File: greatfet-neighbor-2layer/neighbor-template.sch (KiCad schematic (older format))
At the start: 13 parts, among them J1 NEIGHBOR1, J2 NEIGHBOR2, J7 BONUS_ROW, U1 M24C02-FMN6TP

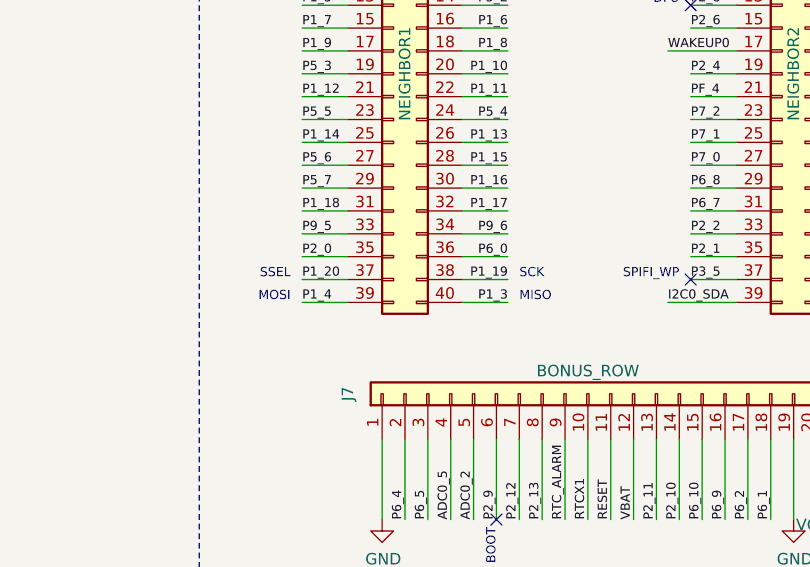
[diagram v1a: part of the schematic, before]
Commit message: adopt OSHWA convention for SPI signal names https://www.oshwa.org/a-resolution-to-redefine-spi-signal-names
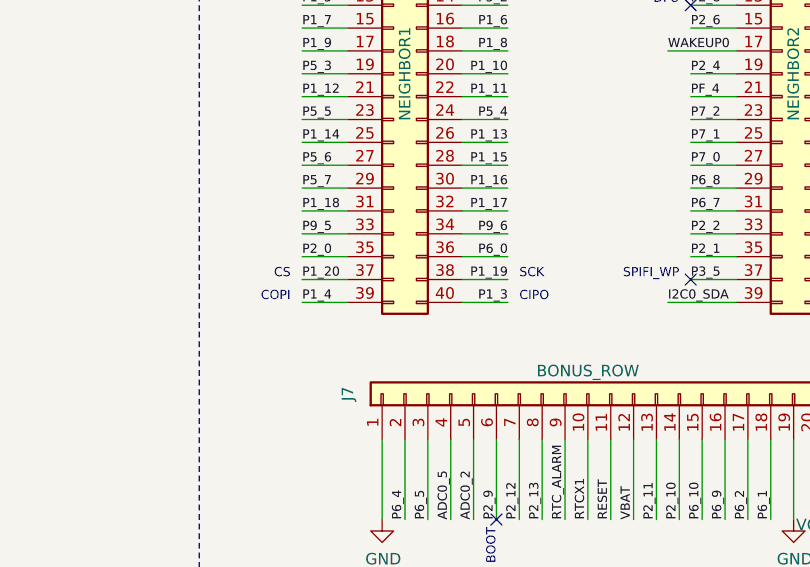
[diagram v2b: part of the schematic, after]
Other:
- note added: "CIPO"
- note added: "COPI"
- note added: "CS"
- note removed: "MISO"
- note removed: "MOSI"
- note removed: "SSEL"
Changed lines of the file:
@@
 P2_0
 Text Notes 14300 2850 0    40   ~ 0
-MISO
+CIPO
 Text Notes 13300 2850 2    40   ~ 0
-MOSI
+COPI
 Text Notes 14300 2750 0    40   ~ 0
 SCK
 Text Notes 13300 2750 2    40   ~ 0
-SSEL
+CS
 Text Label 16050 2850 2    40   ~ 0
 I2C0_SCL

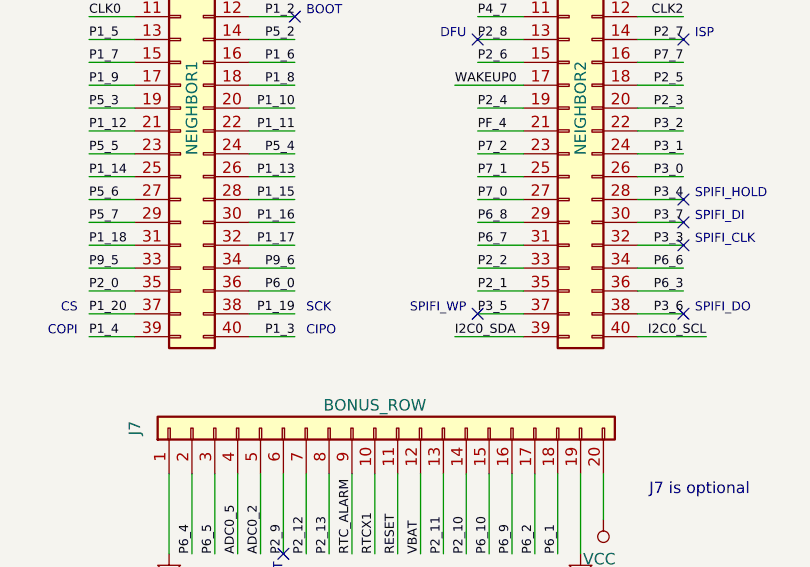
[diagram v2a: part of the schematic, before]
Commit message: label EEPROM_WC
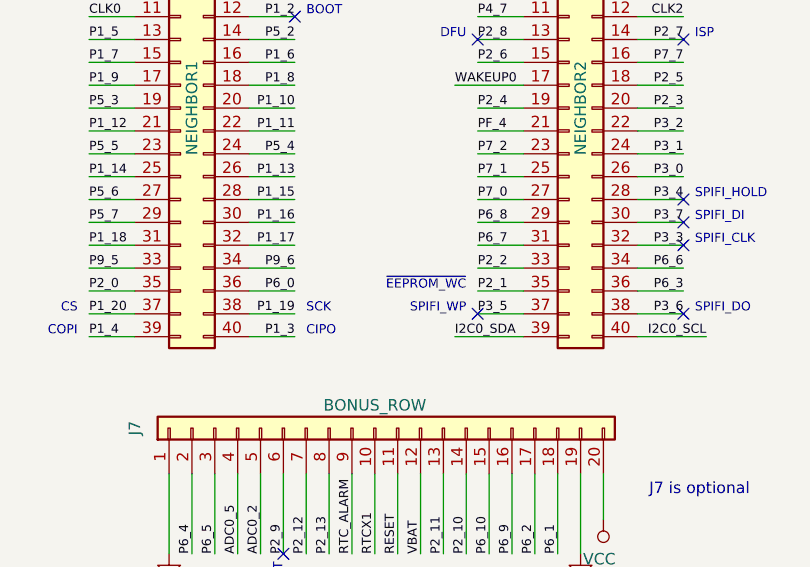
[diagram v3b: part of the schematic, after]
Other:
- note added: "~EEPROM_WC"
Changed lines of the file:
@@
 EESchema Schematic File Version 4
-LIBS:neighbor-template-cache
 EELAYER 30 0
 EELAYER END
@@
 	0    1    1    0
 $EndComp
+Text Notes 15000 2650 2    40   ~ 0
+~EEPROM_WC
 $EndSCHEMATC
